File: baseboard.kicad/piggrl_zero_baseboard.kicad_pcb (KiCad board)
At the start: 2 copper layers, 101 x 43.9 mm, 58 parts, among them P1 PowerBoost 500c, P2 I2C, P3 USB_A, P4 Serial, Q1 IRF7309IPBF, Q3 Q_PMOS_GSD, Q4 MMBT2222, SW1 SW_PUSH, U1 gpio-header_zero, U2 2.2_tft_ili9340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

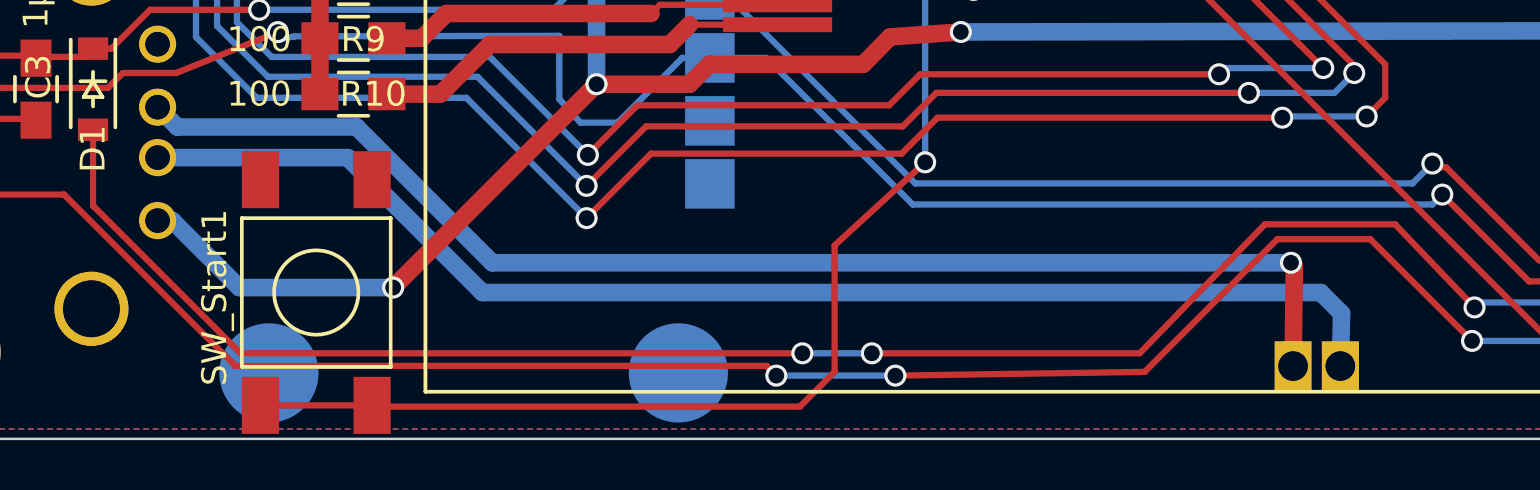
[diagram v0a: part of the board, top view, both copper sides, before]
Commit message: fixed position of solder-holes to the usb-test-pads on the pi-zero
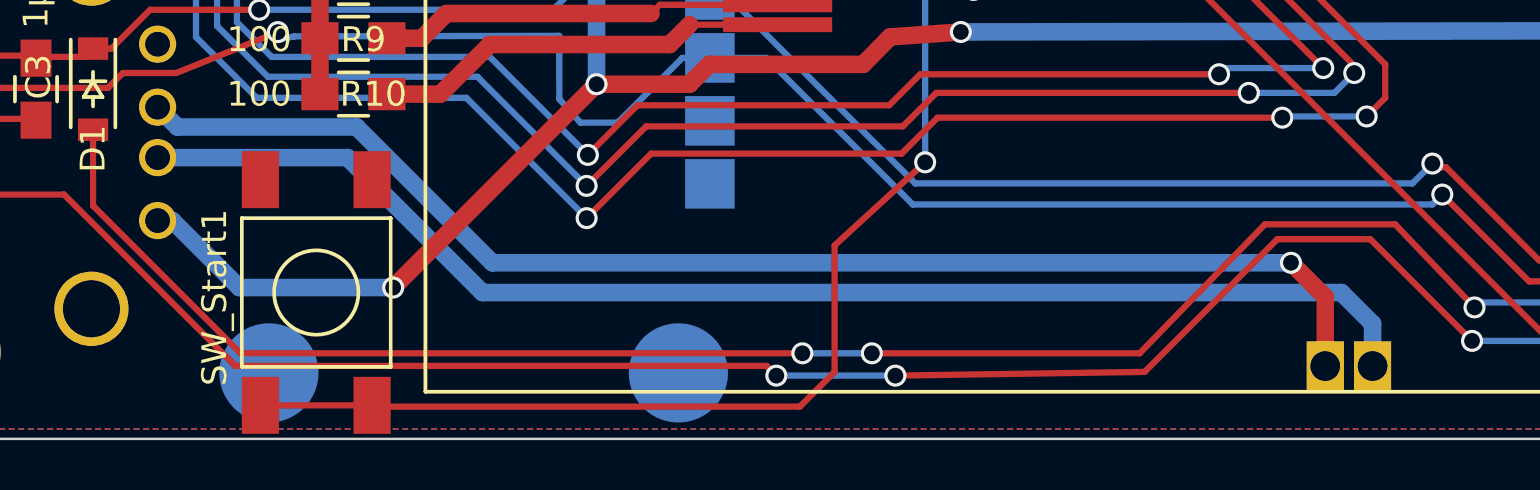
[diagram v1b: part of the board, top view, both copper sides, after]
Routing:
- net Net-(P3-Pad2): track 52.5 -> 53.5 mm
- net Net-(P3-Pad3): track 52.5 -> 53.0 mm
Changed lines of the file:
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@@
     (area 113.016999 90.926522 234 163.200001)
     (thickness 1.6)
-    (drawings 28)
+    (drawings 29)
     (tracks 692)
     (zones 0)
@@
   )
   (setup
-    (last_trace_width 0.254)
+    (last_trace_width 0.708)
     (user_trace_width 0.708)
     (trace_clearance 0.254)
@@
     (mod_text_size 1 1)
     (mod_text_width 0.15)
-    (pad_size 4.064 4.064)
-    (pad_drill 3.1)
+    (pad_size 1.5 2)
+    (pad_drill 1.2)
     (pad_to_mask_clearance 0)
     (aux_axis_origin 0 0)
@@
     (pad 40 smd rect (at 25.4 12.7 180) (size 2 2) (layers B.Cu B.Paste B.Mask)
       (net 59 /btn_7))
-    (pad 45 thru_hole rect (at 10.16 -12.065 180) (size 1.5 2) (drill 1.2) (layers *.Cu *.Mask)
+    (pad 45 thru_hole rect (at 8.86 -12.065 180) (size 1.5 2) (drill 1.2) (layers *.Cu *.Mask)
       (net 19 "Net-(P3-Pad2)"))
-    (pad 46 thru_hole rect (at 12.065 -12.065 180) (size 1.5 2) (drill 1.2) (layers *.Cu *.Mask)
+    (pad 46 thru_hole rect (at 10.77 -12.065 180) (size 1.5 2) (drill 1.2) (layers *.Cu *.Mask)
       (net 18 "Net-(P3-Pad3)"))
   )
@@
     )
   )
+  (dimension 37.6 (width 0.3) (layer Eco2.User)
+    (gr_text "37.600 mm" (at 195.9 157.15) (layer Eco2.User)
+      (effects (font (size 1.5 1.5) (thickness 0.3)))
+    )
+    (feature1 (pts (xy 177.1 151) (xy 177.1 158.5)))
+    (feature2 (pts (xy 214.7 151) (xy 214.7 158.5)))
+    (crossbar (pts (xy 214.7 155.8) (xy 177.1 155.8)))
+    (arrow1a (pts (xy 177.1 155.8) (xy 178.226504 155.213579)))
+    (arrow1b (pts (xy 177.1 155.8) (xy 178.226504 156.386421)))
+    (arrow2a (pts (xy 214.7 155.8) (xy 213.573496 155.213579)))
+    (arrow2b (pts (xy 214.7 155.8) (xy 213.573496 156.386421)))
+  )
   (gr_text 2016-03-05 (at 171.1 120.5) (layer B.SilkS)
     (effects (font (size 1.5 1.5) (thickness 0.3)) (justify mirror))
@@
   (segment (start 192.9 128.8) (end 195.75 128.8) (width 0.254) (layer F.Cu) (net 17))
   (segment (start 183.16 119.06) (end 192.9 128.8) (width 0.254) (layer F.Cu) (net 17))
+  (segment (start 174.8 145.8) (end 176.18 147.18) (width 0.708) (layer F.Cu) (net 18))
+  (segment (start 176.18 147.18) (end 176.18 149.965) (width 0.708) (layer F.Cu) (net 18))
   (segment (start 129.10212 139.52714) (end 129.90212 140.32714) (width 0.708) (layer B.Cu) (net 18))
   (segment (start 137.12714 140.32714) (end 142.6 145.8) (width 0.708) (layer B.Cu) (net 18))
   (segment (start 142.6 145.8) (end 174.8 145.8) (width 0.708) (layer B.Cu) (net 18))
   (via (at 174.8 145.8) (size 0.889) (drill 0.635) (layers F.Cu B.Cu) (net 18))
-  (segment (start 174.8 145.8) (end 174.935 145.935) (width 0.708) (layer F.Cu) (net 18))
-  (segment (start 174.935 145.935) (end 174.885 149.965) (width 0.708) (layer F.Cu) (net 18) (status 20))
   (segment (start 129.90212 140.32714) (end 137.12714 140.32714) (width 0.708) (layer B.Cu) (net 18))
-  (segment (start 129.10212 141.55914) (end 136.75914 141.55914) (width 0.708) (layer B.Cu) (net 19))
-  (segment (start 176.84 147.84) (end 176.79 149.965) (width 0.708) (layer B.Cu) (net 19) (status 20))
-  (segment (start 176 147) (end 176.84 147.84) (width 0.708) (layer B.Cu) (net 19))
-  (segment (start 142.2 147) (end 176 147) (width 0.708) (layer B.Cu) (net 19))
-  (segment (start 136.75914 141.55914) (end 142.2 147) (width 0.708) (layer B.Cu) (net 19))
+  (segment (start 178.09 149.965) (end 178.09 148.257) (width 0.708) (layer B.Cu) (net 19))
+  (segment (start 178.09 148.257) (end 176.833 147) (width 0.708) (layer B.Cu) (net 19))
+  (segment (start 176.833 147) (end 142.2 147) (width 0.708) (layer B.Cu) (net 19))
+  (segment (start 142.2 147) (end 136.75914 141.55914) (width 0.708) (layer B.Cu) (net 19))
+  (segment (start 136.75914 141.55914) (end 129.10212 141.55914) (width 0.708) (layer B.Cu) (net 19))
   (segment (start 189.25 119.228) (end 189.25 121.441998) (width 0.254) (layer B.Cu) (net 20))
   (segment (start 202.24 123.24) (end 202.19 125.2) (width 0.254) (layer B.Cu) (net 20) (status 20))

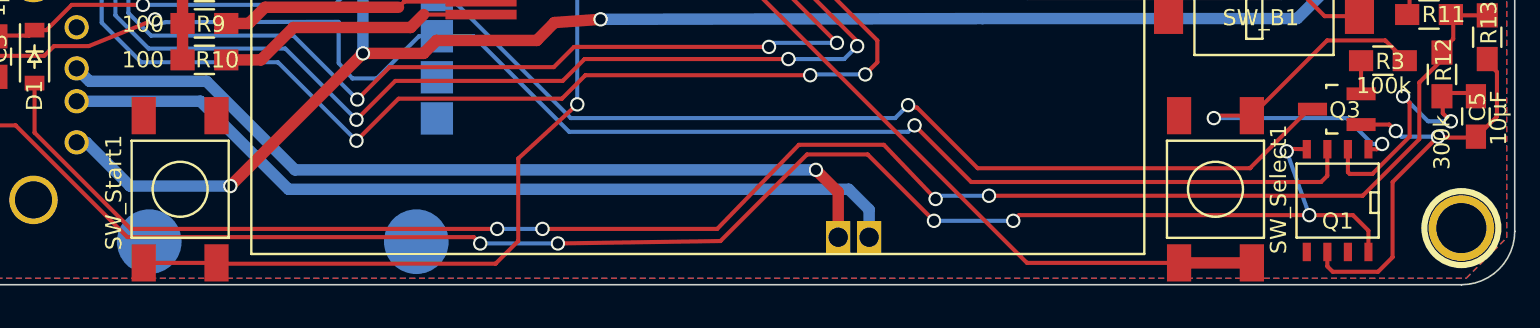
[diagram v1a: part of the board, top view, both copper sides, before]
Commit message: added through-hole pads as clearance for the hdmi-connectors tabs on the raspberry-zero
and rerouted some traces to make way
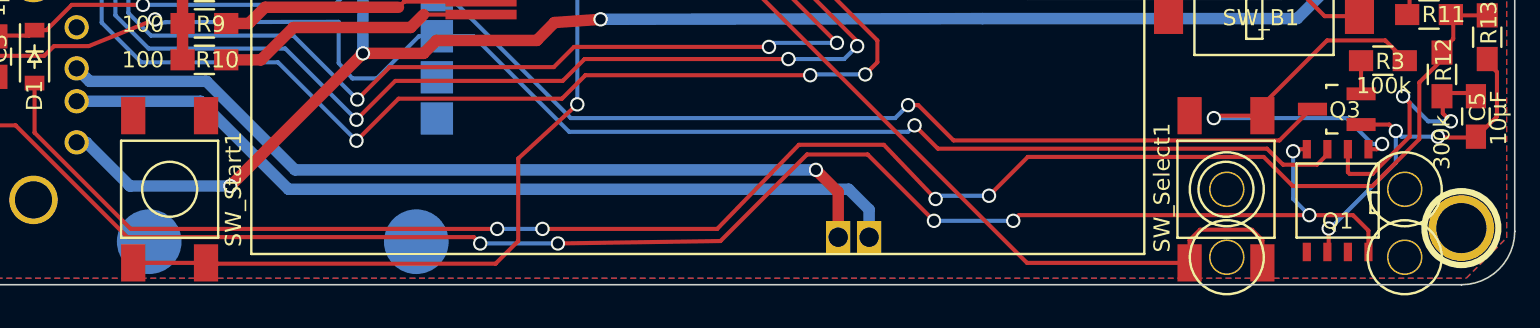
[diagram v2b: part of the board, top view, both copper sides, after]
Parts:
- added REF**: 1pin, Connect:1pin, F.Cu at (211.2, 151.2)
- added REF**: 1pin, Connect:1pin, F.Cu at (211.2, 147.0)
- added REF**: 1pin, Connect:1pin, F.Cu at (200.2, 151.2)
- added REF**: 1pin, Connect:1pin, F.Cu at (200.2, 147.0)
- moved SW_Select1 0.65 mm to (200.2, 147.0)
- moved SW_Start1 0.65 mm to (134.8, 147.0)
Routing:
- net /soft_power_button/Vout: track 27.0 -> 22.2 mm, vias 2 -> 3
- net /btn_8: track 47.5 -> 50.9 mm
- net +BATT: track 103.7 -> 102.0 mm
- net Net-(D1-Pad2): track 107.2 -> 108.7 mm
- net /Enable: track 60.7 -> 59.7 mm
- net Net-(C3-Pad1): track 107.4 -> 106.8 mm

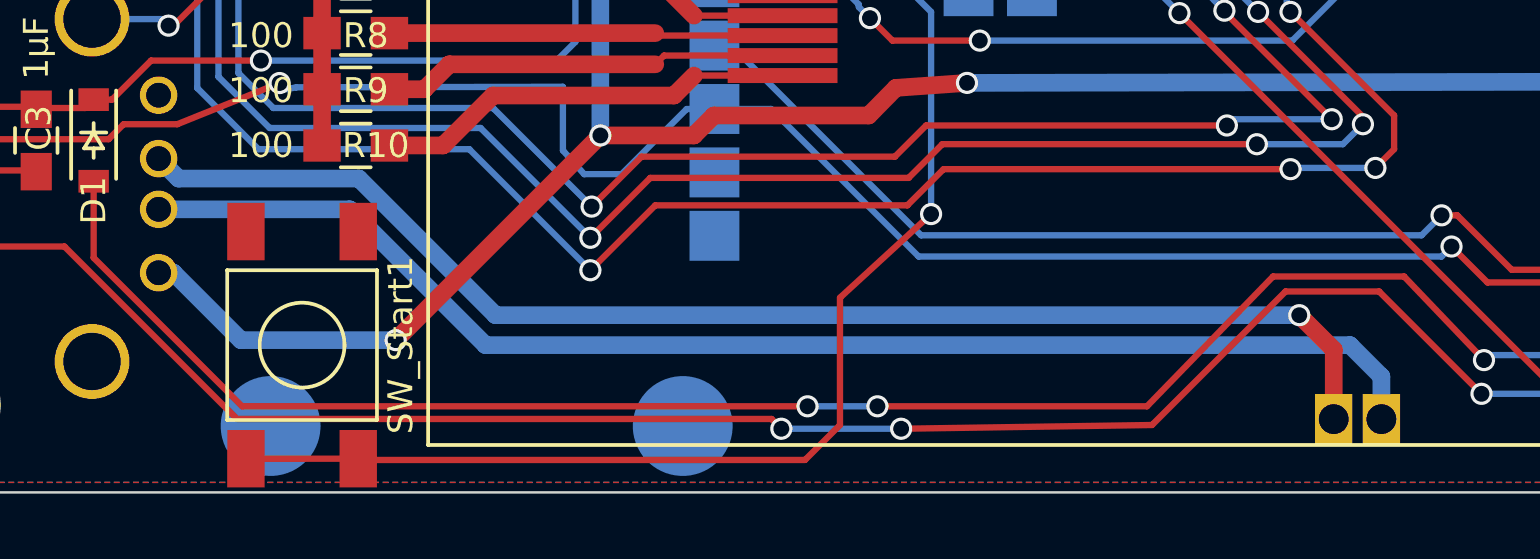
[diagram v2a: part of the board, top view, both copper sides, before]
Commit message: added net_name to usb data lines and rerouted them on the pcb
one less via, and usign kicads wonderfull differential-pair routing tool :-)
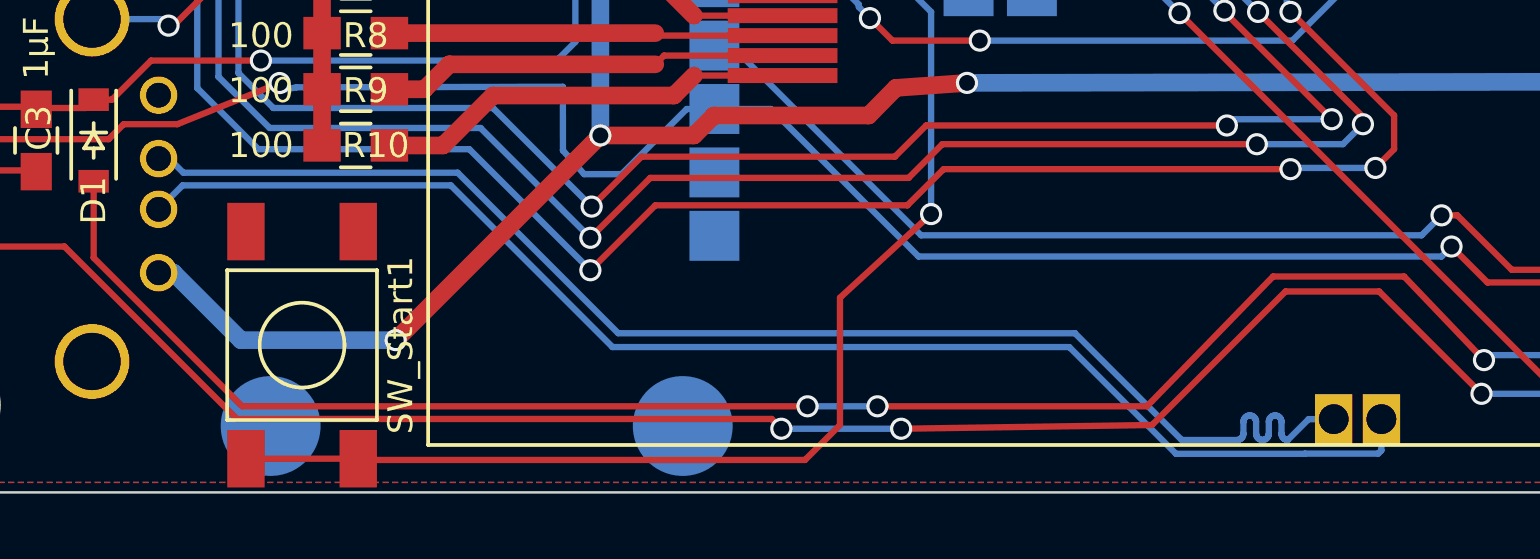
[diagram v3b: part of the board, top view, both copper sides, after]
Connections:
- net Net-(P3-Pad2) renamed /USB_D-
- net Net-(P3-Pad3) renamed /USB_D+
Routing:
- net /USB_D+: track 53.0 -> 55.1 mm, vias 1 -> 0
- net /USB_D-: track 53.5 -> 55.1 mm

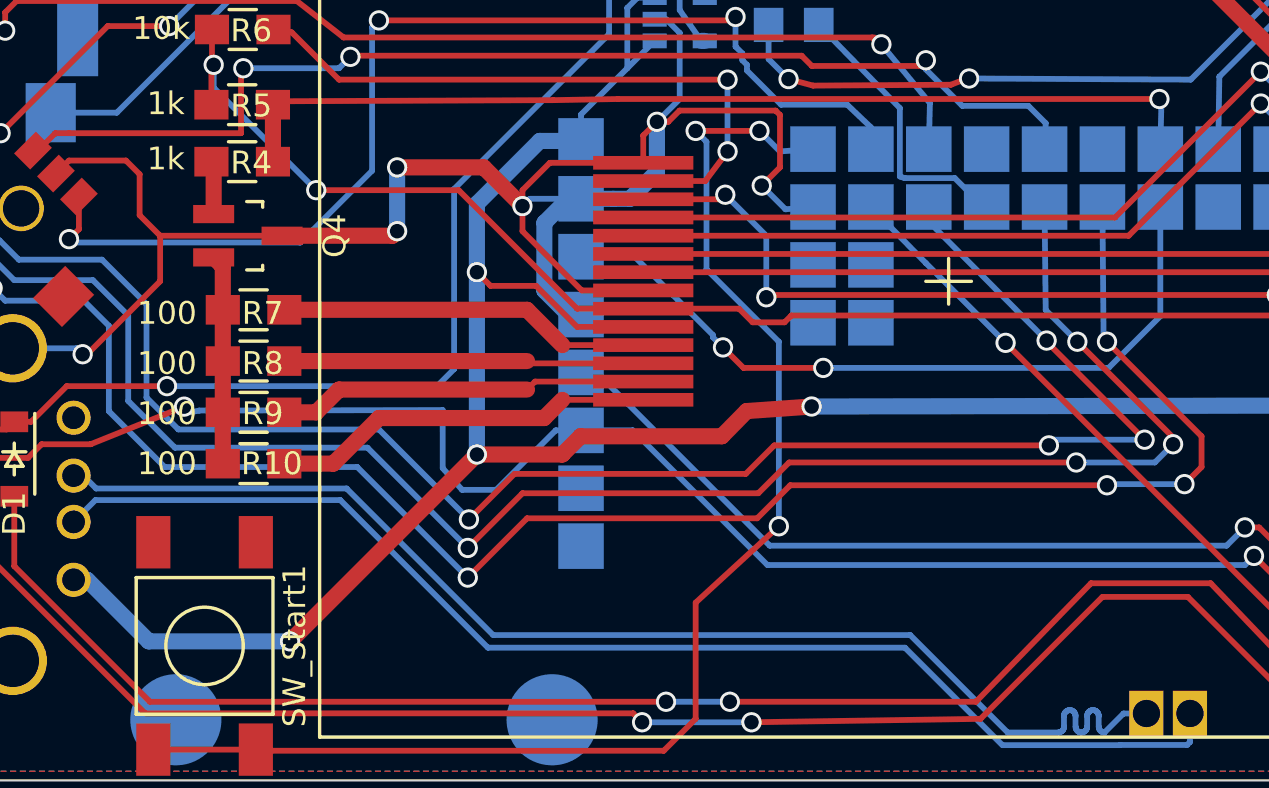
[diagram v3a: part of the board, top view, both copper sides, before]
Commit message: bugfix: backlicht transistor pinout was BCE instead of common BEC
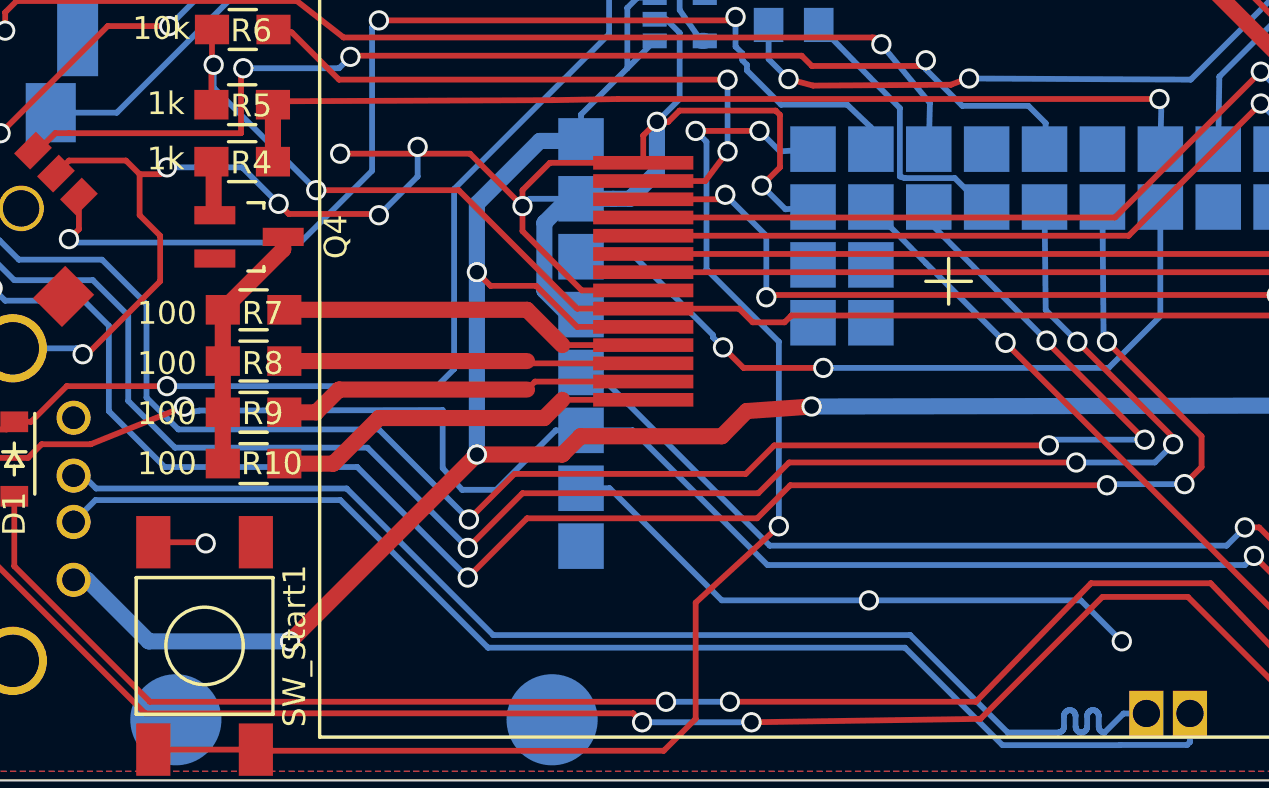
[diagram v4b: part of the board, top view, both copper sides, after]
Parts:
- moved Q4 0.07 mm to (136.8, 129.1)
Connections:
- Q4 pad 2: Net-(Q4-Pad2) -> GND
- Q4 pad 3: GND -> Net-(Q4-Pad3)
- R10 pad 2: Net-(Q4-Pad2) -> Net-(Q4-Pad3)
- R7 pad 2: Net-(Q4-Pad2) -> Net-(Q4-Pad3)
- R8 pad 2: Net-(Q4-Pad2) -> Net-(Q4-Pad3)
- R9 pad 2: Net-(Q4-Pad2) -> Net-(Q4-Pad3)
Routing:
- net GND: track 141.4 -> 174.9 mm, vias 13 -> 19
- net Net-(Q4-Pad3): track 0.00 -> 11.0 mm
- net Net-(Q4-Pad2): track 9.22 -> 0.00 mm
